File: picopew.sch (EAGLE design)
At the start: 16 parts, among them U1 IS31FL3733-TQLS4

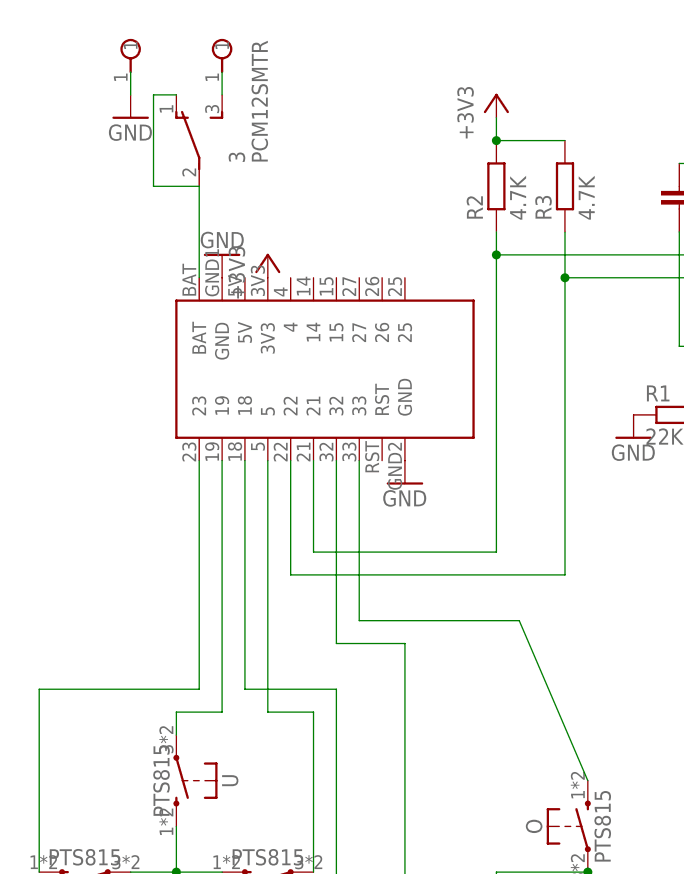
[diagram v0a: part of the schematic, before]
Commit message: Add JST connector footprint for those who want to connect their battery that way.
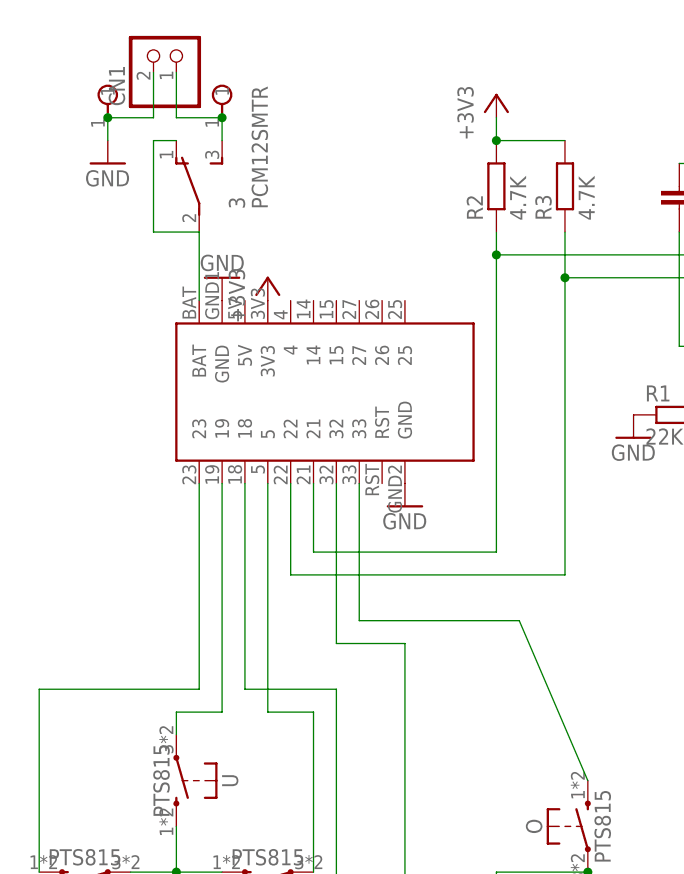
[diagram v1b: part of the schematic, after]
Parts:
- added CN1: (no value), cwpackage:JST_2PIN-SMT-RA
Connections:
- net GND: now also CN1.1
- net N$31: now also CN1.2
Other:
- moved on the sheet: 3
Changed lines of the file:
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@@
 <part name="5" library="cwpackage" deviceset="SINGLEPAD" device=""/>
 <part name="GND7" library="supply1" deviceset="GND" device=""/>
+<part name="CN1" library="cwpackage" deviceset="JST_2PIN" device="-SMT-RA"/>
 </parts>
 <sheets>
@@
 <instance part="U1" gate="G$1" x="50.8" y="50.8"/>
 <instance part="1" gate="G$1" x="137.16" y="43.18"/>
-<instance part="2" gate="G$1" x="-12.7" y="50.8"/>
-<instance part="GND1" gate="1" x="-2.54" y="38.1"/>
-<instance part="GND2" gate="1" x="-22.86" y="63.5" rot="R180"/>
+<instance part="2" gate="G$1" x="-12.7" y="48.26"/>
+<instance part="GND1" gate="1" x="-2.54" y="35.56"/>
+<instance part="GND2" gate="1" x="-22.86" y="60.96" rot="R180"/>
 <instance part="GND3" gate="1" x="35.56" y="10.16"/>
-<instance part="+3V1" gate="G$1" x="-17.78" y="63.5"/>
+<instance part="+3V1" gate="G$1" x="-17.78" y="60.96"/>
 <instance part="+3V2" gate="G$1" x="35.56" y="83.82"/>
 <instance part="L" gate="G$1" x="-38.1" y="-7.62" rot="R90"/>
@@
 <instance part="+3V3" gate="G$1" x="7.62" y="81.28"/>
 <instance part="C1" gate="G$1" x="27.94" y="71.12"/>
-<instance part="3" gate="G$1" x="-25.4" y="76.2"/>
-<instance part="4" gate="G$1" x="-22.86" y="86.36" rot="R90"/>
-<instance part="5" gate="G$1" x="-33.02" y="86.36" rot="R90"/>
-<instance part="GND7" gate="1" x="-33.02" y="78.74"/>
+<instance part="3" gate="G$1" x="-25.4" y="71.12"/>
+<instance part="4" gate="G$1" x="-22.86" y="81.28" rot="R90"/>
+<instance part="5" gate="G$1" x="-35.56" y="81.28" rot="R90"/>
+<instance part="GND7" gate="1" x="-35.56" y="73.66"/>
+<instance part="CN1" gate="G$1" x="-27.94" y="86.36" rot="R90"/>
 </instances>
 <busses>
@@
 <segment>
 <pinref part="2" gate="G$1" pin="21"/>
-<wire x1="-12.7" y1="40.64" x2="-12.7" y2="30.48" width="0.1524" layer="91"/>
+<wire x1="-12.7" y1="38.1" x2="-12.7" y2="30.48" width="0.1524" layer="91"/>
 <wire x1="-12.7" y1="30.48" x2="7.62" y2="30.48" width="0.1524" layer="91"/>
 <pinref part="U1" gate="G$1" pin="SDA"/>
@@
 <segment>
 <pinref part="2" gate="G$1" pin="22"/>
-<wire x1="-15.24" y1="40.64" x2="-15.24" y2="27.94" width="0.1524" layer="91"/>
+<wire x1="-15.24" y1="38.1" x2="-15.24" y2="27.94" width="0.1524" layer="91"/>
 <wire x1="-15.24" y1="27.94" x2="15.24" y2="27.94" width="0.1524" layer="91"/>
 <pinref part="U1" gate="G$1" pin="SCL"/>
@@
 <pinref part="GND7" gate="1" pin="GND"/>
 <pinref part="5" gate="G$1" pin="1"/>
-<wire x1="-33.02" y1="81.28" x2="-33.02" y2="83.82" width="0.1524" layer="91"/>
+<wire x1="-35.56" y1="76.2" x2="-35.56" y2="78.74" width="0.1524" layer="91"/>
+<pinref part="CN1" gate="G$1" pin="1"/>
+<wire x1="-35.56" y1="78.74" x2="-30.48" y2="78.74" width="0.1524" layer="91"/>
+<wire x1="-30.48" y1="78.74" x2="-30.48" y2="83.82" width="0.1524" layer="91"/>
+<junction x="-35.56" y="78.74"/>
 </segment>
 <segment>
@@
 <wire x1="10.16" y1="22.86" x2="-7.62" y2="22.86" width="0.1524" layer="91"/>
 <pinref part="2" gate="G$1" pin="33"/>
-<wire x1="-7.62" y1="22.86" x2="-7.62" y2="40.64" width="0.1524" layer="91"/>
+<wire x1="-7.62" y1="22.86" x2="-7.62" y2="38.1" width="0.1524" layer="91"/>
 <pinref part="O" gate="G$1" pin="S"/>
 <wire x1="10.16" y1="22.86" x2="17.78" y2="5.08" width="0.1524" layer="91"/>
@@
 <pinref part="2" gate="G$1" pin="32"/>
 <wire x1="-2.54" y1="20.32" x2="-10.16" y2="20.32" width="0.1524" layer="91"/>
-<wire x1="-10.16" y1="20.32" x2="-10.16" y2="40.64" width="0.1524" layer="91"/>
+<wire x1="-10.16" y1="20.32" x2="-10.16" y2="38.1" width="0.1524" layer="91"/>
 <pinref part="X" gate="G$1" pin="P"/>
 <wire x1="7.62" y1="-17.78" x2="-2.54" y2="-17.78" width="0.1524" layer="91"/>
@@
 <pinref part="3" gate="G$1" pin="S"/>
 <pinref part="4" gate="G$1" pin="1"/>
-<wire x1="-22.86" y1="81.28" x2="-22.86" y2="83.82" width="0.1524" layer="91"/>
+<wire x1="-22.86" y1="76.2" x2="-22.86" y2="78.74" width="0.1524" layer="91"/>
+<pinref part="CN1" gate="G$1" pin="2"/>
+<wire x1="-22.86" y1="78.74" x2="-27.94" y2="78.74" width="0.1524" layer="91"/>
+<wire x1="-27.94" y1="78.74" x2="-27.94" y2="83.82" width="0.1524" layer="91"/>
+<junction x="-22.86" y="78.74"/>
 </segment>
 </net>
@@
 <segment>
 <pinref part="2" gate="G$1" pin="5"/>
-<wire x1="-17.78" y1="40.64" x2="-17.78" y2="12.7" width="0.1524" layer="91"/>
+<wire x1="-17.78" y1="38.1" x2="-17.78" y2="12.7" width="0.1524" layer="91"/>
 <pinref part="R" gate="G$1" pin="P"/>
 <wire x1="-17.78" y1="12.7" x2="-12.7" y2="12.7" width="0.1524" layer="91"/>
@@
 <pinref part="2" gate="G$1" pin="18"/>
 <wire x1="-10.16" y1="15.24" x2="-20.32" y2="15.24" width="0.1524" layer="91"/>
-<wire x1="-20.32" y1="15.24" x2="-20.32" y2="40.64" width="0.1524" layer="91"/>
+<wire x1="-20.32" y1="15.24" x2="-20.32" y2="38.1" width="0.1524" layer="91"/>
 </segment>
 </net>
@@
 <pinref part="2" gate="G$1" pin="19"/>
 <wire x1="-27.94" y1="12.7" x2="-22.86" y2="12.7" width="0.1524" layer="91"/>
-<wire x1="-22.86" y1="12.7" x2="-22.86" y2="40.64" width="0.1524" layer="91"/>
+<wire x1="-22.86" y1="12.7" x2="-22.86" y2="38.1" width="0.1524" layer="91"/>
 </segment>
 </net>
@@
 <segment>
 <pinref part="2" gate="G$1" pin="23"/>
-<wire x1="-25.4" y1="40.64" x2="-25.4" y2="15.24" width="0.1524" layer="91"/>
+<wire x1="-25.4" y1="38.1" x2="-25.4" y2="15.24" width="0.1524" layer="91"/>
 <pinref part="L" gate="G$1" pin="S"/>
 <wire x1="-25.4" y1="15.24" x2="-43.18" y2="15.24" width="0.1524" layer="91"/>
@@
 <segment>
 <pinref part="3" gate="G$1" pin="O"/>
-<wire x1="-27.94" y1="81.28" x2="-30.48" y2="81.28" width="0.1524" layer="91"/>
-<wire x1="-30.48" y1="81.28" x2="-30.48" y2="71.12" width="0.1524" layer="91"/>
+<wire x1="-27.94" y1="76.2" x2="-30.48" y2="76.2" width="0.1524" layer="91"/>
+<wire x1="-30.48" y1="76.2" x2="-30.48" y2="66.04" width="0.1524" layer="91"/>
 <pinref part="2" gate="G$1" pin="BAT"/>
 <pinref part="3" gate="G$1" pin="P"/>
-<wire x1="-25.4" y1="60.96" x2="-25.4" y2="71.12" width="0.1524" layer="91"/>
-<wire x1="-30.48" y1="71.12" x2="-25.4" y2="71.12" width="0.1524" layer="91"/>
-</segment>
-</net>
+<wire x1="-25.4" y1="58.42" x2="-25.4" y2="66.04" width="0.1524" layer="91"/>
+<wire x1="-30.48" y1="66.04" x2="-25.4" y2="66.04" width="0.1524" layer="91"/>
+</segment>
+</net>
